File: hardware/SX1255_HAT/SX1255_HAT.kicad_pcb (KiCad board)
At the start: 2 copper layers, 65 x 30 mm, 32 parts, among them IC1 SX1255, J1 TX_SMA, J2 RX_SMA, J3 RPi Zero, Y1 32MHz

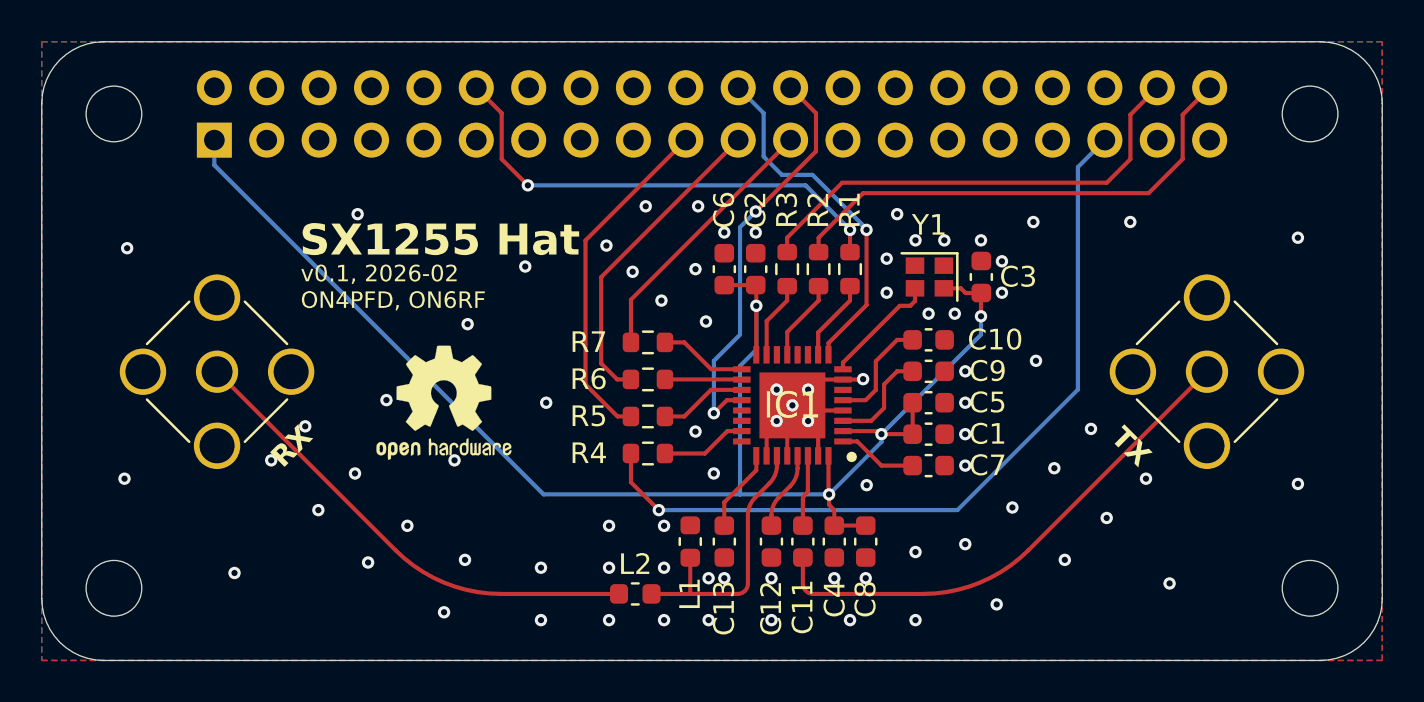
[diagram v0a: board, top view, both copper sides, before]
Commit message: Added Tx filters, EEPROM, modified for soapy-sx compat
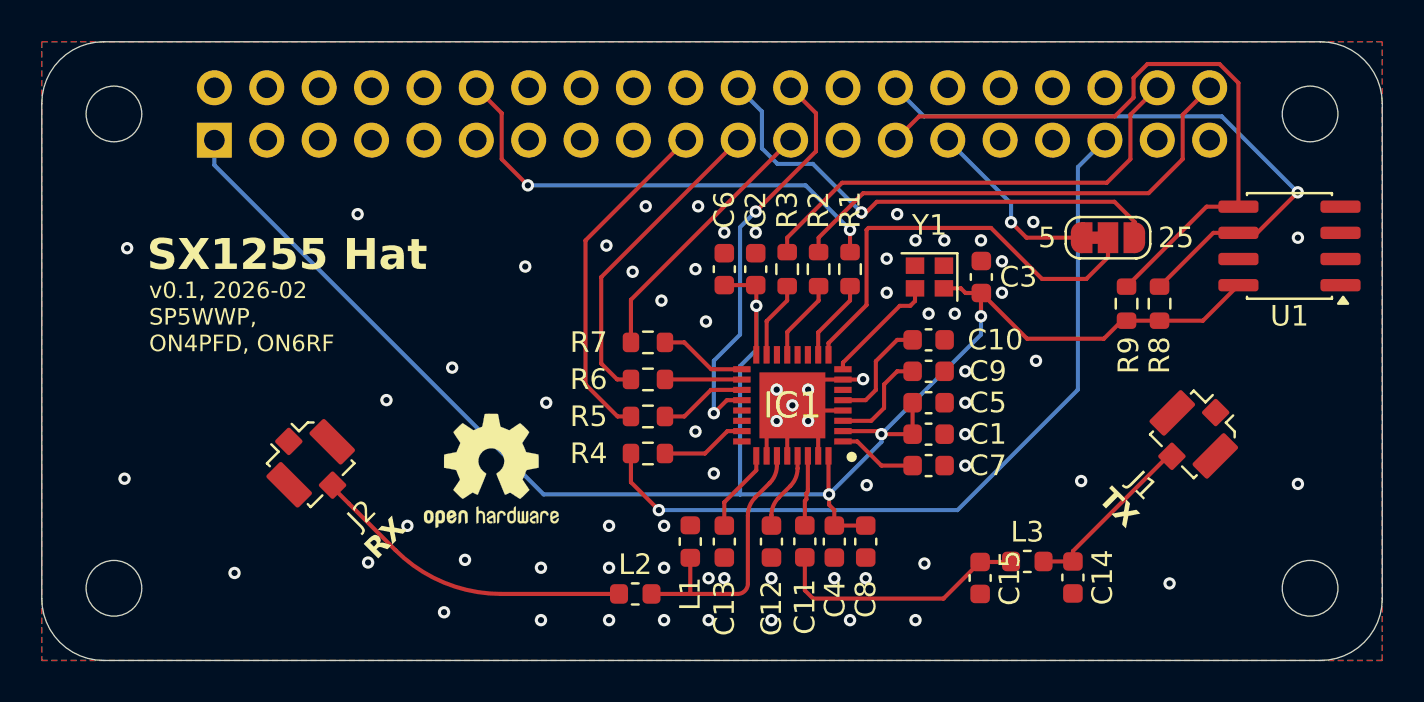
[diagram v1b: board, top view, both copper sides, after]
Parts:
- added C14: 12p, Capacitor_SMD:C_0603_1608Metric, F.Cu at (150.0, 96.0)
- added C15: 12p, Capacitor_SMD:C_0603_1608Metric, F.Cu at (145.5, 96.0)
- added JP1: RST_SEL, Jumper:SolderJumper-3_P1.3mm_Bridged12_RoundedPad1.0x1.5mm_NumberLabels, F.Cu at (151.7, 79.5)
- added L3: 39n, Inductor_SMD:L_0603_1608Metric, F.Cu at (147.8, 95.2)
- added R8: 3K9, Resistor_SMD:R_0603_1608Metric, F.Cu at (154.2, 82.7)
- added R9: 3K9, Resistor_SMD:R_0603_1608Metric, F.Cu at (152.6, 82.7)
- added U1: 24LC256, Package_SO:SOIC-8_3.9x4.9mm_P1.27mm, F.Cu at (160.5, 79.9)
- J1: value TX_SMA -> TX; footprint Connector_Coaxial:SMA_Amphenol_901-144_Vertical -> Connector_Coaxial:U.FL_Molex_MCRF_73412-0110_Vertical
- J2: value RX_SMA -> RX; footprint Connector_Coaxial:SMA_Amphenol_901-144_Vertical -> Connector_Coaxial:U.FL_Molex_MCRF_73412-0110_Vertical
- moved J2 6.35 mm to (113.0, 90.4)
- moved SYM1 4.02 mm to (121.8, 90.8)
- moved J1 3.11 mm to (155.9, 89.0), turned to -45 degrees
- moved C11 0.09 mm to (137.0, 94.2)
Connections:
- C11 pad 2: Net-(J1-In) -> Net-(C11-Pad2)
- J3 pad 22: /RST -> /GPIO25
- J3 pad 27: unconnected-(J3-Pin_27-Pad27) -> /ID_SD
- J3 pad 28: unconnected-(J3-Pin_28-Pad28) -> /ID_SC
- J3 pad 29: unconnected-(J3-Pin_29-Pad29) -> /GPIO5
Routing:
- net /ID_SD: track 0.00 -> 32.1 mm
- net /ID_SC: track 0.00 -> 30.5 mm, vias 0 -> 1
- net /GPIO25: track 0.00 -> 24.5 mm, vias 0 -> 1
- net Net-(J1-In): track 25.2 -> 8.81 mm
- net +3V3: track 76.8 -> 91.2 mm
- net Net-(C11-Pad2): track 0.00 -> 12.5 mm
- net /GPIO5: track 0.00 -> 8.96 mm, vias 0 -> 1
- net Net-(J2-In): track 23.6 -> 15.8 mm
- net /RST: track 17.2 -> 21.0 mm, vias 1 -> 0
- net GND: vias 81 -> 69
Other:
- board text added: "v0.1, 2026-02 SP5WWP, ON4PFD, ON6RF"
- board text removed: "v0.1, 2026-02 ON4PFD, ON6RF"

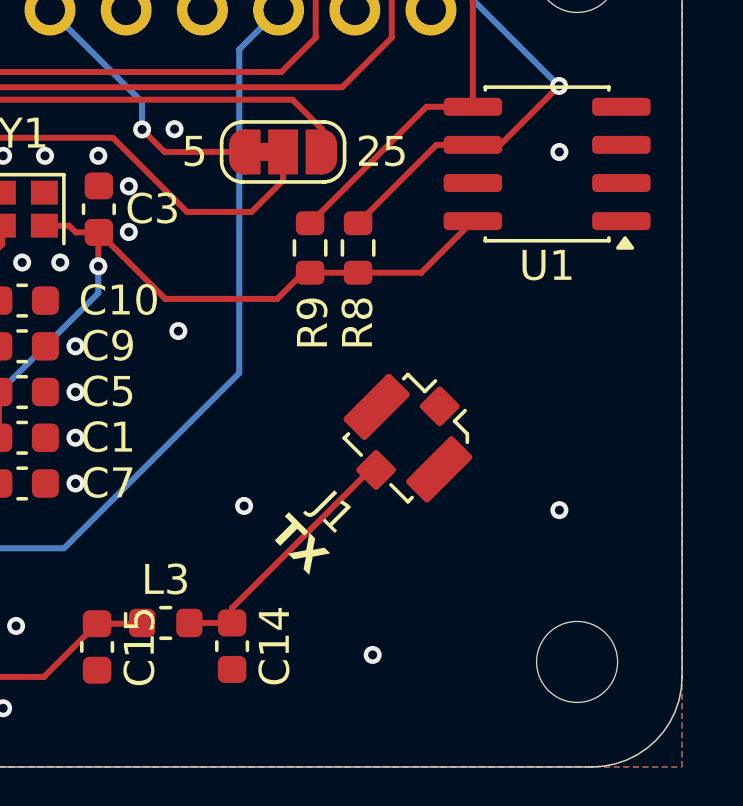
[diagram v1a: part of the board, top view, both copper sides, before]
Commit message: Added decoupling for EEPROM and WP pin
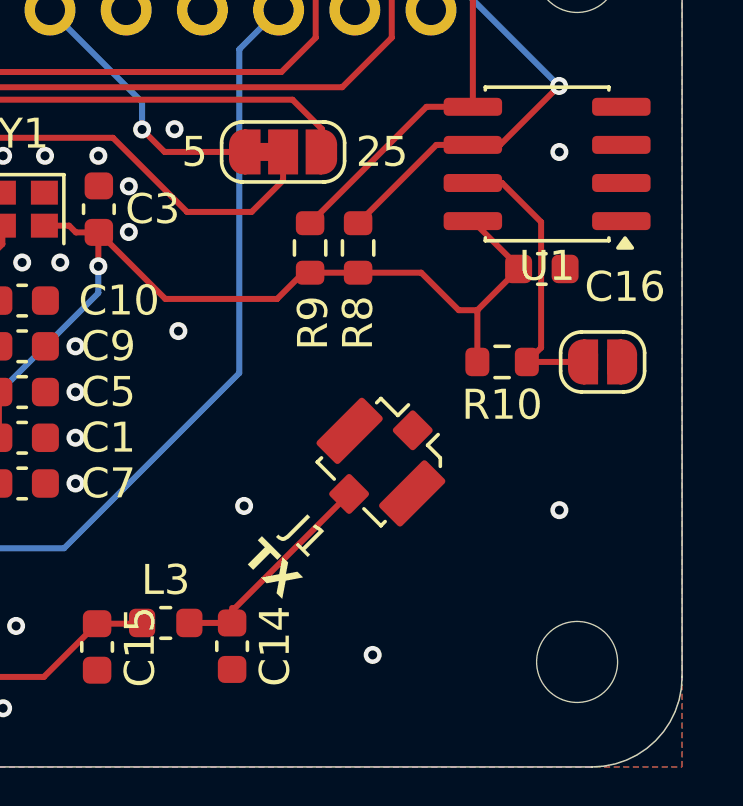
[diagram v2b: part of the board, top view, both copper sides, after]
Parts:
- added C16: 10n, Capacitor_SMD:C_0603_1608Metric, F.Cu at (160.3, 83.4)
- added JP2: WP, Jumper:SolderJumper-2_P1.3mm_Open_RoundedPad1.0x1.5mm, F.Cu at (162.3, 86.5)
- added R10: 3K9, Resistor_SMD:R_0603_1608Metric, F.Cu at (159.0, 86.5)
- C14, C15: value 12p -> 6.8p
- L3: value 39n -> 33n
- moved J1 1.20 mm to (155.0, 89.8)
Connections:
- U1 pad 7: unconnected-(U1-WP-Pad7) -> Net-(JP2-A)
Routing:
- net Net-(JP2-A): track 0.00 -> 9.55 mm
- net +3V3: track 91.2 -> 97.1 mm
- net Net-(J1-In): track 8.81 -> 8.02 mm

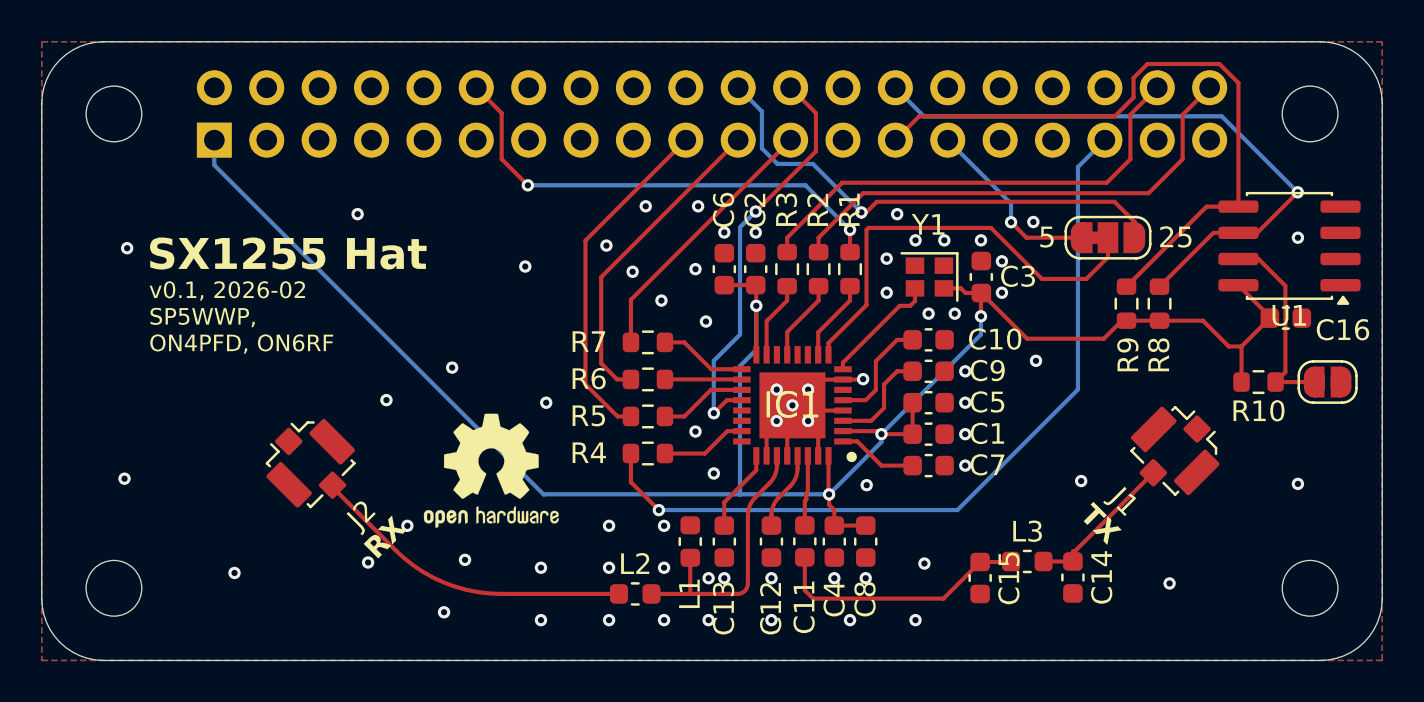
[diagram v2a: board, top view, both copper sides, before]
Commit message: added DRU, modified component placement, updated schematic
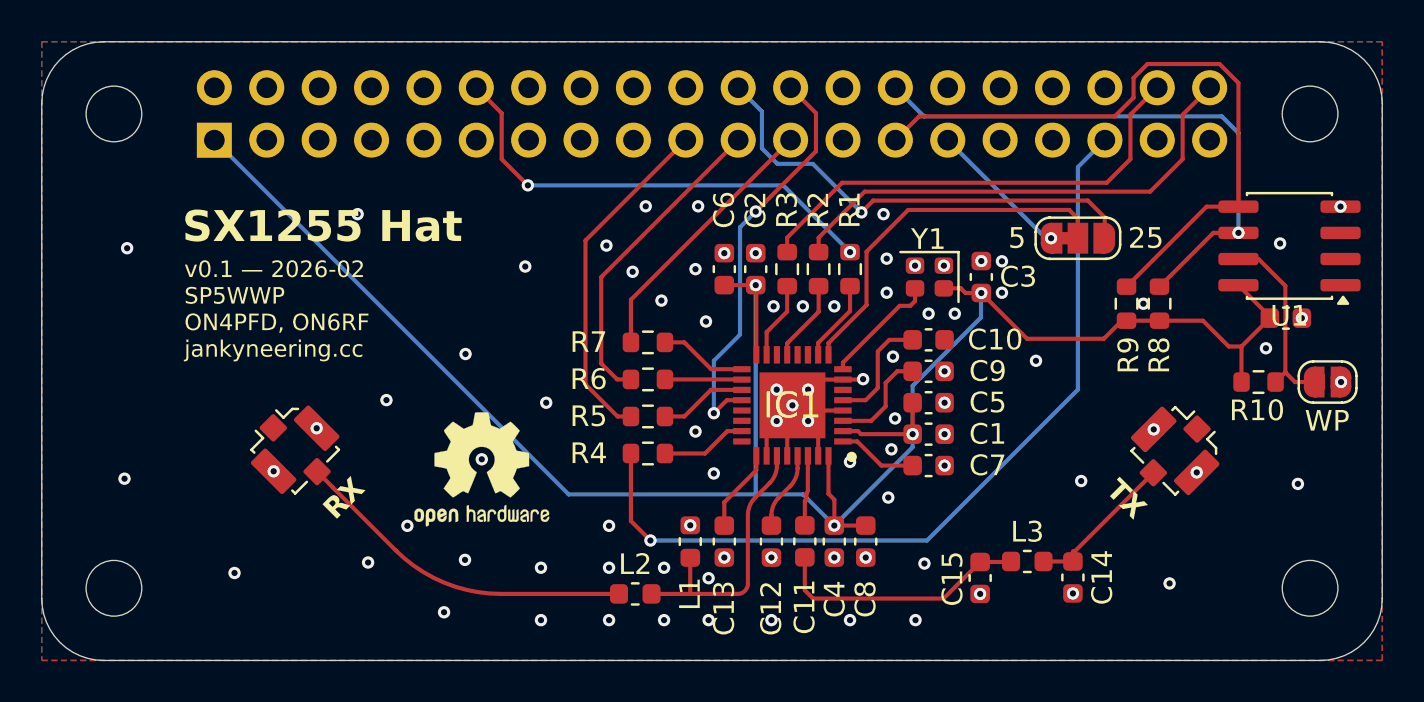
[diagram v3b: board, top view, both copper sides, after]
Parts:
- moved JP1 1.46 mm to (150.2, 79.5)
- moved J2 1.00 mm to (112.3, 89.8)
- moved SYM1 0.47 mm to (121.3, 90.7)
- turned R10 to 0 degrees
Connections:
- J3 pad 14: unconnected-(J3-Pin_14-Pad14) -> GND
- J3 pad 2: unconnected-(J3-Pin_2-Pad2) -> +5V
- J3 pad 20: unconnected-(J3-Pin_20-Pad20) -> GND
- J3 pad 25: unconnected-(J3-Pin_25-Pad25) -> GND
- J3 pad 30: unconnected-(J3-Pin_30-Pad30) -> GND
- J3 pad 34: unconnected-(J3-Pin_34-Pad34) -> GND
- J3 pad 4: unconnected-(J3-Pin_4-Pad4) -> +5V
- J3 pad 6: unconnected-(J3-Pin_6-Pad6) -> GND
- J3 pad 9: unconnected-(J3-Pin_9-Pad9) -> GND
- R10 pad 1: Net-(JP2-A) -> +3V3
- R10 pad 2: +3V3 -> Net-(JP2-A)
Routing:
- net /ID_SC: track 30.5 -> 27.3 mm
- net /RST: track 21.0 -> 18.0 mm
- net /DIO2: track 38.7 -> 41.0 mm
- net +3V3: track 97.1 -> 99.3 mm
- net /GPIO5: track 8.96 -> 6.98 mm
- net /GPIO25: track 24.5 -> 22.9 mm
- net Net-(J2-In): track 15.8 -> 16.8 mm
- net /OUT: track 23.4 -> 22.7 mm
- net GND: vias 69 -> 86
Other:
- board text added: "WP"
- board text added: "v0.1 — 2026-02 SP5WWP ON4PFD, ON6RF jankyneering.cc"
- board text removed: "v0.1, 2026-02 SP5WWP, ON4PFD, ON6RF"

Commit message: added fabrication files
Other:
- board text added: "RST_SEL"
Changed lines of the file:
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@@
+		)
+	)
+	(gr_text "RST_SEL"
+		(at 150.241 77.6478 0)
+		(layer "F.SilkS")
+		(effects
+			(font
+				(size 1 1)
+				(thickness 0.15)
+			)
 		)
 	)
